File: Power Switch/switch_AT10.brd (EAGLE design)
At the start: 17.9 x 13.2 mm, 16 parts, among them U2 ATTINY10-TS8R

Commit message: updates
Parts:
- R2: value 330 -> 100
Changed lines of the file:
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@@
 <drawing>
 <settings>
-<setting alwaysvectorfont="yes"/>
+<setting alwaysvectorfont="no"/>
 <setting verticaltext="up"/>
 </settings>
 <grid distance="50" unitdist="mil" unit="mil" style="lines" multiple="1" display="no" altdistance="5" altunitdist="mil" altunit="mil"/>
 <layers>
-<layer number="1" name="Top" color="4" fill="1" visible="no" active="yes"/>
+<layer number="1" name="Top" color="4" fill="1" visible="yes" active="yes"/>
 <layer number="2" name="Route2" color="1" fill="3" visible="no" active="no"/>
 <layer number="3" name="Route3" color="4" fill="3" visible="no" active="no"/>
@@
 <layer number="14" name="Route14" color="1" fill="6" visible="no" active="no"/>
 <layer number="15" name="Route15" color="4" fill="6" visible="no" active="no"/>
-<layer number="16" name="Bottom" color="1" fill="1" visible="yes" active="yes"/>
+<layer number="16" name="Bottom" color="1" fill="1" visible="no" active="yes"/>
 <layer number="17" name="Pads" color="2" fill="1" visible="yes" active="yes"/>
 <layer number="18" name="Vias" color="2" fill="1" visible="yes" active="yes"/>
 <layer number="19" name="Unrouted" color="6" fill="1" visible="yes" active="yes"/>
 <layer number="20" name="Dimension" color="24" fill="1" visible="yes" active="yes"/>
-<layer number="21" name="tPlace" color="7" fill="1" visible="no" active="yes"/>
-<layer number="22" name="bPlace" color="7" fill="1" visible="yes" active="yes"/>
-<layer number="23" name="tOrigins" color="15" fill="1" visible="no" active="yes"/>
-<layer number="24" name="bOrigins" color="15" fill="1" visible="yes" active="yes"/>
-<layer number="25" name="tNames" color="7" fill="1" visible="no" active="yes"/>
-<layer number="26" name="bNames" color="7" fill="1" visible="yes" active="yes"/>
+<layer number="21" name="tPlace" color="7" fill="1" visible="yes" active="yes"/>
+<layer number="22" name="bPlace" color="7" fill="1" visible="no" active="yes"/>
+<layer number="23" name="tOrigins" color="15" fill="1" visible="yes" active="yes"/>
+<layer number="24" name="bOrigins" color="15" fill="1" visible="no" active="yes"/>
+<layer number="25" name="tNames" color="7" fill="1" visible="yes" active="yes"/>
+<layer number="26" name="bNames" color="7" fill="1" visible="no" active="yes"/>
 <layer number="27" name="tValues" color="7" fill="1" visible="no" active="yes"/>
 <layer number="28" name="bValues" color="7" fill="1" visible="no" active="yes"/>
@@
 <layer number="37" name="tTest" color="7" fill="1" visible="no" active="yes"/>
 <layer number="38" name="bTest" color="7" fill="1" visible="no" active="yes"/>
-<layer number="39" name="tKeepout" color="4" fill="11" visible="no" active="yes"/>
-<layer number="40" name="bKeepout" color="1" fill="11" visible="yes" active="yes"/>
-<layer number="41" name="tRestrict" color="4" fill="10" visible="no" active="yes"/>
-<layer number="42" name="bRestrict" color="1" fill="10" visible="yes" active="yes"/>
+<layer number="39" name="tKeepout" color="4" fill="11" visible="yes" active="yes"/>
+<layer number="40" name="bKeepout" color="1" fill="11" visible="no" active="yes"/>
+<layer number="41" name="tRestrict" color="4" fill="10" visible="yes" active="yes"/>
+<layer number="42" name="bRestrict" color="1" fill="10" visible="no" active="yes"/>
 <layer number="43" name="vRestrict" color="2" fill="10" visible="no" active="yes"/>
 <layer number="44" name="Drills" color="7" fill="1" visible="no" active="yes"/>
@@
 <layer number="49" name="Reference" color="7" fill="1" visible="no" active="yes"/>
 <layer number="50" name="dxf" color="7" fill="1" visible="no" active="no"/>
-<layer number="51" name="tDocu" color="7" fill="1" visible="no" active="yes"/>
-<layer number="52" name="bDocu" color="7" fill="1" visible="yes" active="yes"/>
+<layer number="51" name="tDocu" color="7" fill="1" visible="yes" active="yes"/>
+<layer number="52" name="bDocu" color="7" fill="1" visible="no" active="yes"/>
 <layer number="53" name="tGND_GNDA" color="7" fill="9" visible="no" active="no"/>
 <layer number="54" name="bGND_GNDA" color="1" fill="9" visible="no" active="no"/>
@@
 <attribute name="VALUE" x="9.069" y="97.127" size="1.27" layer="27" rot="R270"/>
 </element>
-<element name="R2" library="rcl" library_urn="urn:adsk.eagle:library:334" package="R0603" package3d_urn="urn:adsk.eagle:package:23555/2" value="330" x="10.668" y="92.329" smashed="yes" rot="R180">
+<element name="R2" library="rcl" library_urn="urn:adsk.eagle:library:334" package="R0603" package3d_urn="urn:adsk.eagle:package:23555/2" value="100" x="10.668" y="92.329" smashed="yes" rot="R180">
 <attribute name="NAME" x="10.16" y="93.091" size="0.762" layer="25" font="vector" ratio="10"/>
 <attribute name="SPICEPREFIX" value="R" x="17.018" y="92.329" size="1.778" layer="27" rot="R180" display="off"/>

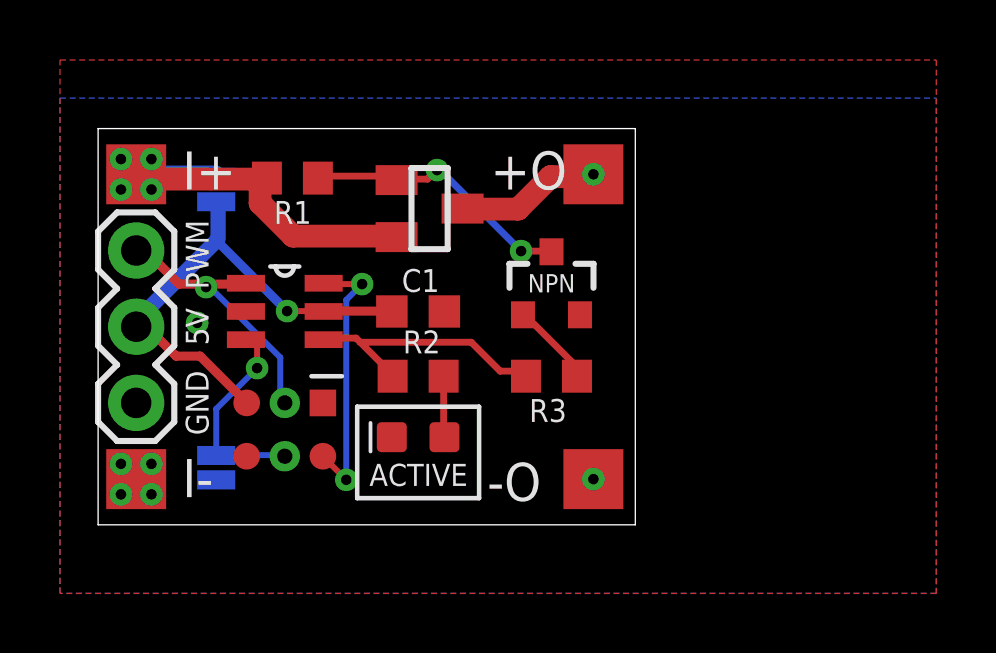
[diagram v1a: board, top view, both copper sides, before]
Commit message: PCB updates (jumper distance) and a new RGB mini board
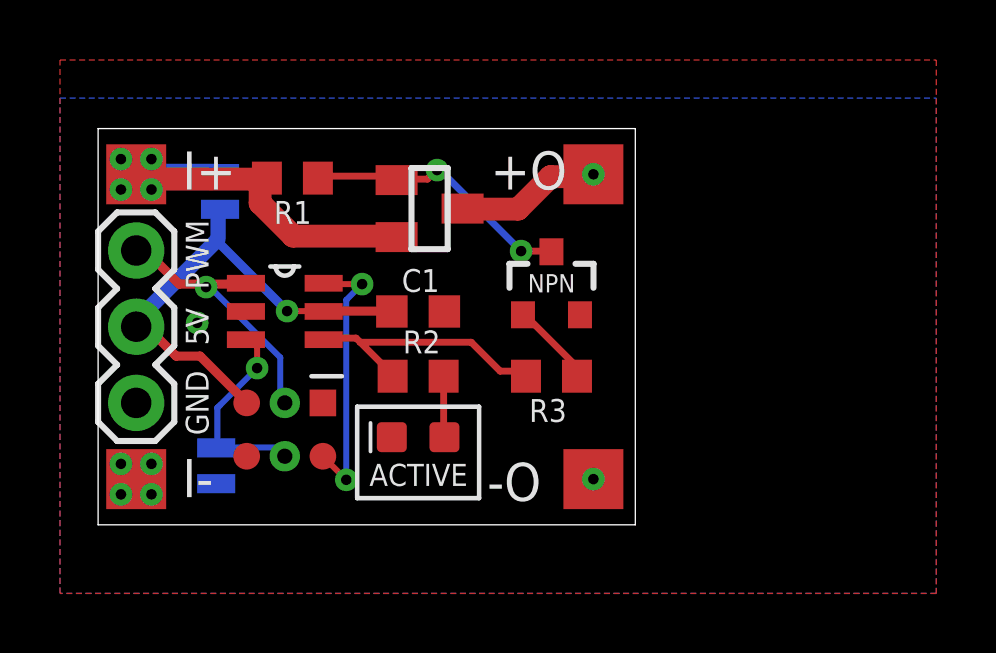
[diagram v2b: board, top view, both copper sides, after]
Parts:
- removed INV, INV1: PWM INV JUMPER, SparkFun-Jumpers:SMT-JUMPER_2_NO_NO-SILK
- added JP1, JP2: JUMPER-SMT_2_NO_NO-SILK, SparkFun-Jumpers:SMT-JUMPER_2_NO_NO-SILK
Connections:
- net 5V: now also JP1.2; no longer INV1.2
- net GND: now also JP2.1; no longer INV.1
- net SCK: now also JP2.2; no longer INV.2
- net VCC: now also JP1.1; no longer INV1.1
